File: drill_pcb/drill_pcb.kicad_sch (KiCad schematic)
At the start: 38 parts, among them SW1 RPi reset, U1 PCA9306, U2 Pico, U3 L7805, U4 IFX007T, U5 IFX007T, U6 ACS712xLCTR-20A

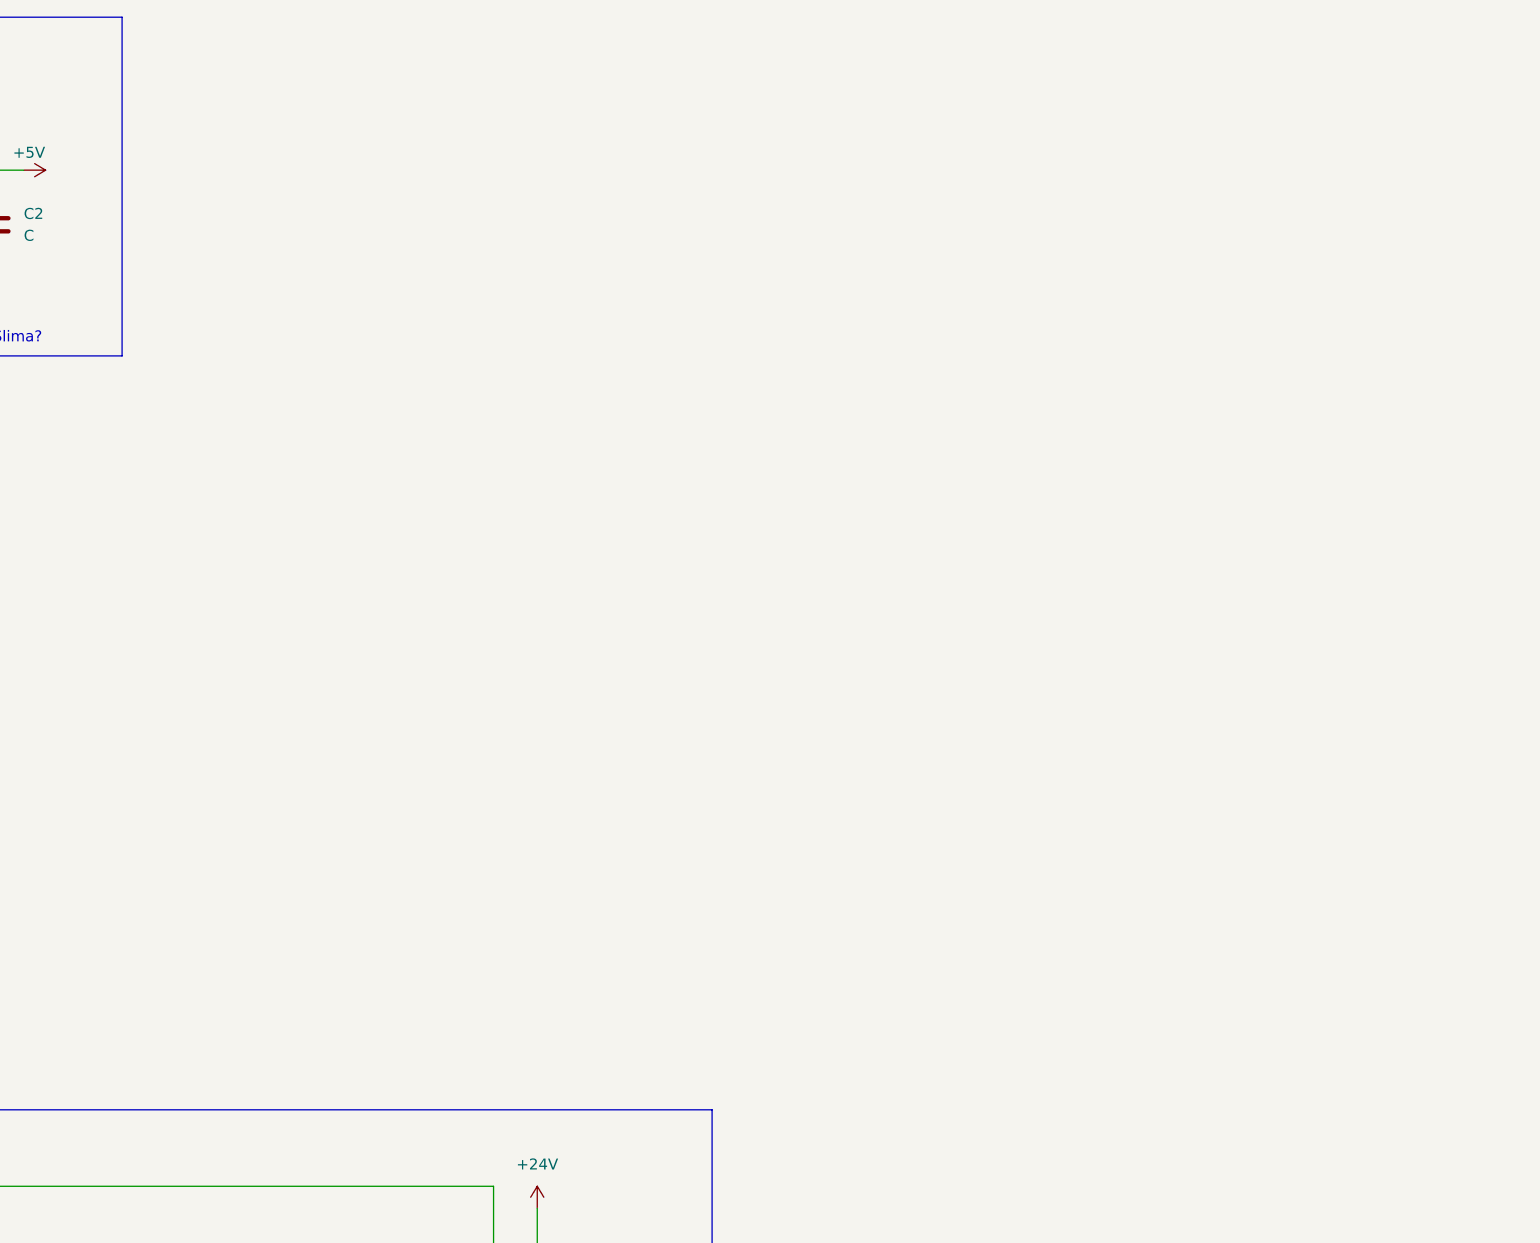
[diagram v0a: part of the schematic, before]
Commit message: storage and weighing scheme added
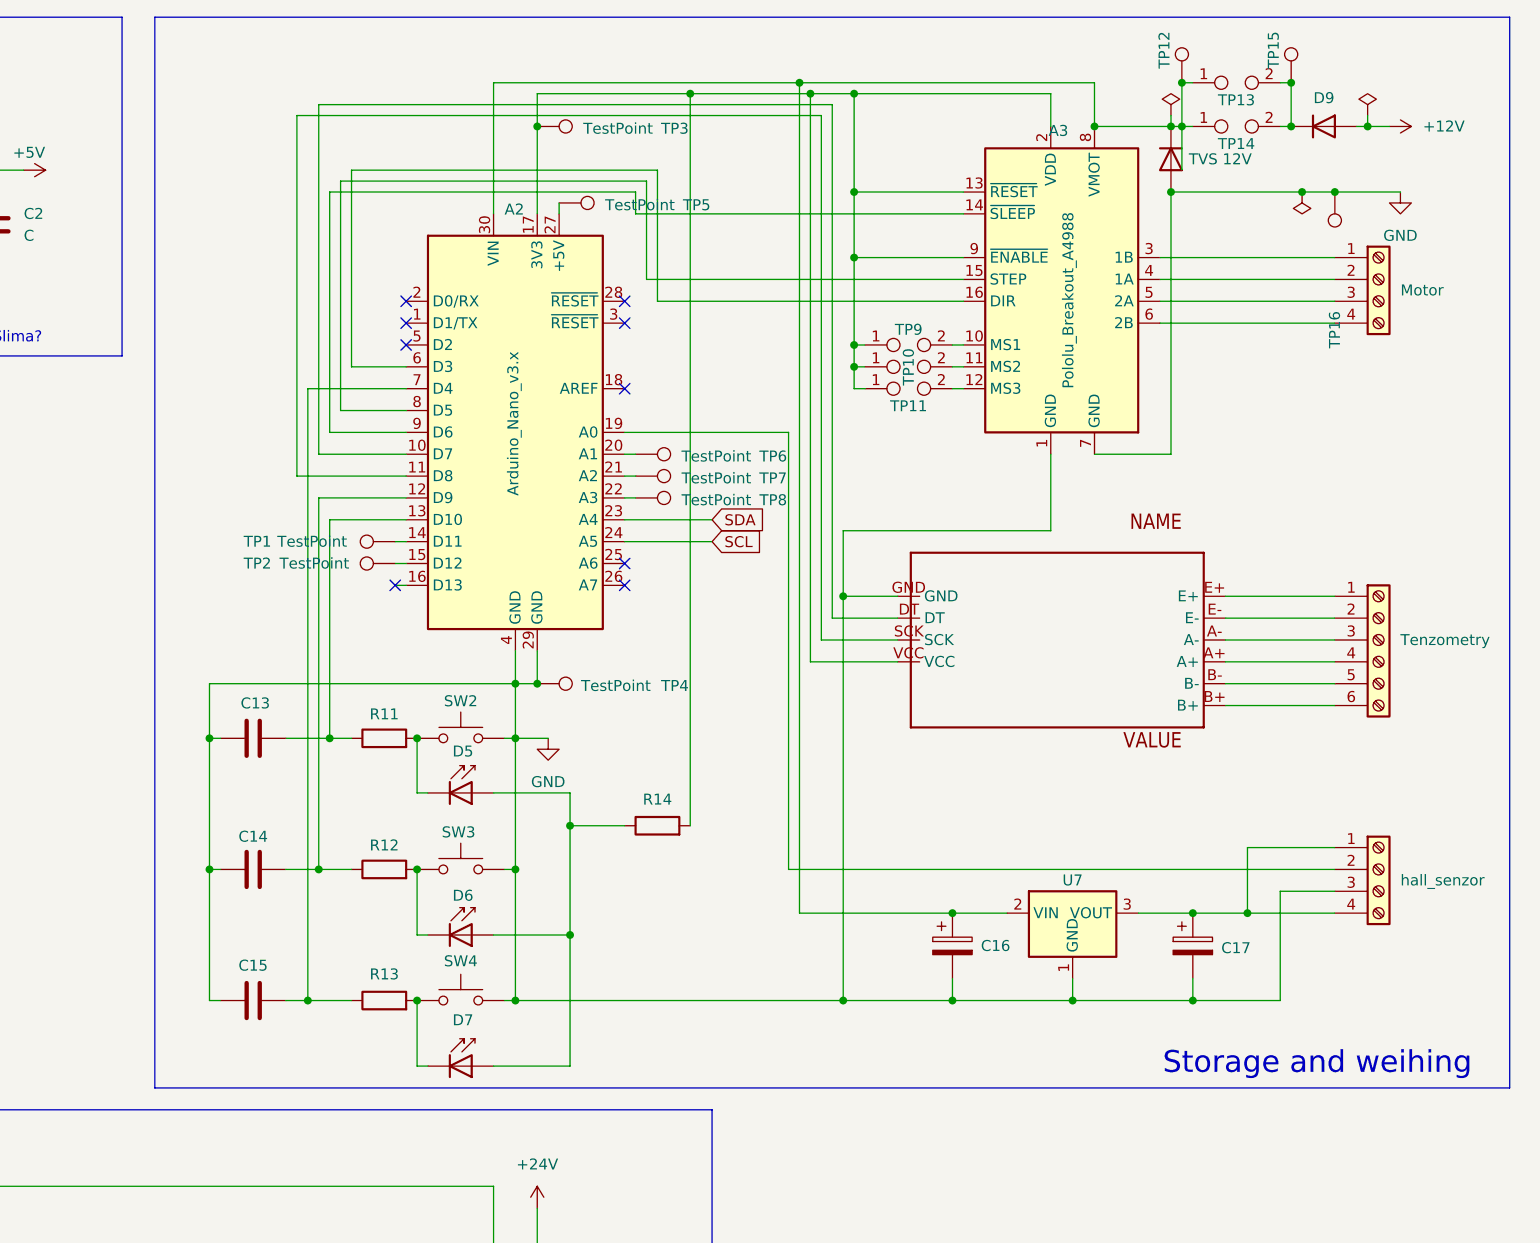
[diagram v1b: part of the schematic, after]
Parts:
- added 111: ~, hx711footp:HX711, symbol HX711:HX711A
- added A2: Arduino_Nano_v3.x, Module:Arduino_Nano, symbol MCU_Module:Arduino_Nano_v3.x
- added A3: Pololu_Breakout_A4988, Module:Pololu_Breakout-16_15.2x20.3mm, symbol Driver_Motor:Pololu_Breakout_A4988
- added C13, C14, C15: 10n, Capacitor_THT:C_Disc_D4.7mm_W2.5mm_P5.00mm, symbol Device:C
- added C16, C17: C_Polarized, Capacitor_THT:CP_Radial_D5.0mm_P2.50mm, symbol Device:C_Polarized
- added D5, D6, D7: SFH4550, LED_THT:LED_D5.0mm_IRGrey, symbol LED:SFH4550
- added D8: TVS 12V, Diode_THT:D_DO-41_SOD81_P10.16mm_Horizontal, symbol Diode:1N4007
- added D9: 1N4007, Diode_THT:D_DO-41_SOD81_P10.16mm_Horizontal, symbol Diode:1N4007
- added Motor, hall_senzor: Screw_Terminal_01x04, TerminalBlock_TE-Connectivity:TerminalBlock_TE_282834-4_1x04_P2.54mm_Horizontal, symbol Connector:Screw_Terminal_01x04
- added R11, R12, R13, R14: 10k, Resistor_THT:R_Axial_DIN0207_L6.3mm_D2.5mm_P10.16mm_Horizontal, symbol Device:R
- added SW2, SW3, SW4: SW_Push, Button_Switch_THT:SW_PUSH_6mm, symbol Switch:SW_Push
- added TP1, TP12, TP15, TP16, TP2, TP3, TP4, TP5, TP6, TP7, TP8: TestPoint, TestPoint:TestPoint_Pad_1.5x1.5mm, symbol Connector:TestPoint
- added TP10, TP11, TP14, TP9: TestPoint_2Pole, Capacitor_SMD:C_0504_1310Metric_Pad0.83x1.28mm_HandSolder, symbol Connector:TestPoint_2Pole
- added TP13: TestPoint_2Pole, Resistor_THT:R_Axial_DIN0309_L9.0mm_D3.2mm_P12.70mm_Horizontal, symbol Connector:TestPoint_2Pole
- added Tenzometry: Screw_Terminal_01x06, TerminalBlock_TE-Connectivity:TerminalBlock_TE_282834-6_1x06_P2.54mm_Horizontal, symbol Connector:Screw_Terminal_01x06
- added U7: HT75xx-1-SOT89, Package_TO_SOT_THT:TO-92L_Inline, symbol Regulator_Linear:HT75xx-1-SOT89
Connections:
- net +12V: now also D9.2 (A)
- net GND: now also 111.GND, A2.29 (GND), A2.4 (GND), A3.1 (GND), A3.7 (GND), C13.1, C14.1, C15.1, C16.2, C17.2, D8.2 (A), SW2.2, SW3.2, SW4.2, TP16.1, TP4.1, U7.1 (GND), hall_senzor.3 (Pin_3)
- net SCL: now also A2.24 (A5)
- net SDA: now also A2.23 (A4)
- new net: D7.1 (K), R13.2, SW4.1
- new net: D9.1 (K), TP13.2, TP14.2, TP15.1
- new net: A2.27 (+5V), TP5.1
- new net: A2.30 (VIN), A3.8 (VMOT), C16.1, D8.1 (K), TP12.1, TP13.1, TP14.1, U7.2 (VIN)
- new net: C17.1, U7.3 (VOUT), hall_senzor.1 (Pin_1), hall_senzor.4 (Pin_4)
- new net: D5.2 (A), D6.2 (A), D7.2 (A), R14.1
- new net: 111.VCC, A2.17 (3V3), A3.13 (~{RESET}), A3.2 (VDD), A3.9 (~{ENABLE}), R14.2, TP10.1, TP11.1, TP3.1, TP9.1
- new net: D5.1 (K), R11.2, SW2.1
- new net: A2.13 (D10), C13.2, R11.1
- new net: A2.22 (A3), TP8.1
- new net: A2.12 (D9), C14.2, R12.1
- new net: D6.1 (K), R12.2, SW3.1
- new net: 111.E+, Tenzometry.1 (Pin_1)
- new net: 111.E-, Tenzometry.2 (Pin_2)
- new net: 111.A-, Tenzometry.3 (Pin_3)
- new net: 111.A+, Tenzometry.4 (Pin_4)
- new net: 111.B-, Tenzometry.5 (Pin_5)
- new net: 111.B+, Tenzometry.6 (Pin_6)
- new net: A2.14 (D11), TP1.1
- new net: A2.15 (D12), TP2.1
- new net: A3.11 (MS2), TP10.2
- new net: 111.DT, A2.10 (D7)
- new net: 111.SCK, A2.11 (D8)
- new net: A2.19 (A0), hall_senzor.2 (Pin_2)
- new net: A2.21 (A2), TP7.1
- new net: A3.3 (1B), Motor.1 (Pin_1)
- new net: A3.4 (1A), Motor.2 (Pin_2)
- new net: A3.5 (2A), Motor.3 (Pin_3)
- new net: A3.6 (2B), Motor.4 (Pin_4)
- new net: A3.10 (MS1), TP9.2
- new net: A3.12 (MS3), TP11.2
- new net: A2.9 (D6), A3.14 (~{SLEEP})
- new net: A2.8 (D5), A3.15 (STEP)
- new net: A2.6 (D3), A3.16 (DIR)
- new net: A2.7 (D4), C15.2, R13.1
- new net: A2.20 (A1), TP6.1
- no-connect marks 55 -> 64
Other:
- note added: "Storage and weihing"
